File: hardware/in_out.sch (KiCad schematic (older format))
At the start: 33 parts, among them P2 CONN_8, Q4 MMBT2222AT, Q5 MMBT2222AT, Q6 MMBT2222AT, Q7 MMBT2222AT, U6 LTC2635_MSE

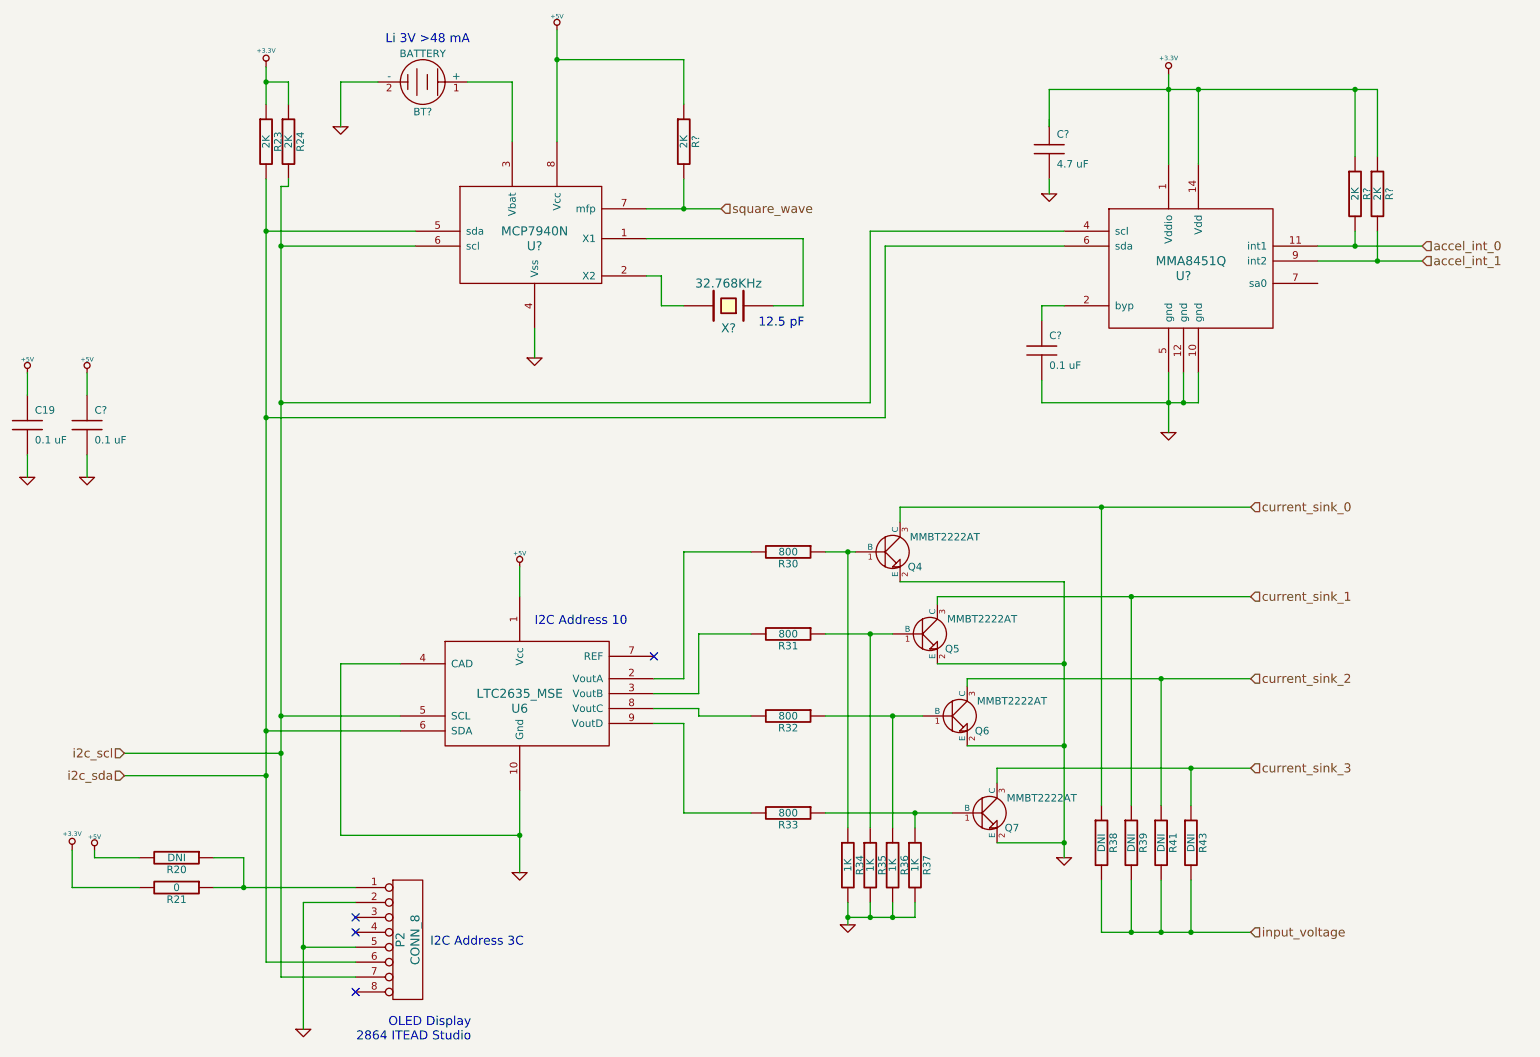
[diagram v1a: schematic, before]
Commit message: fixed some ERCs and simplified reset
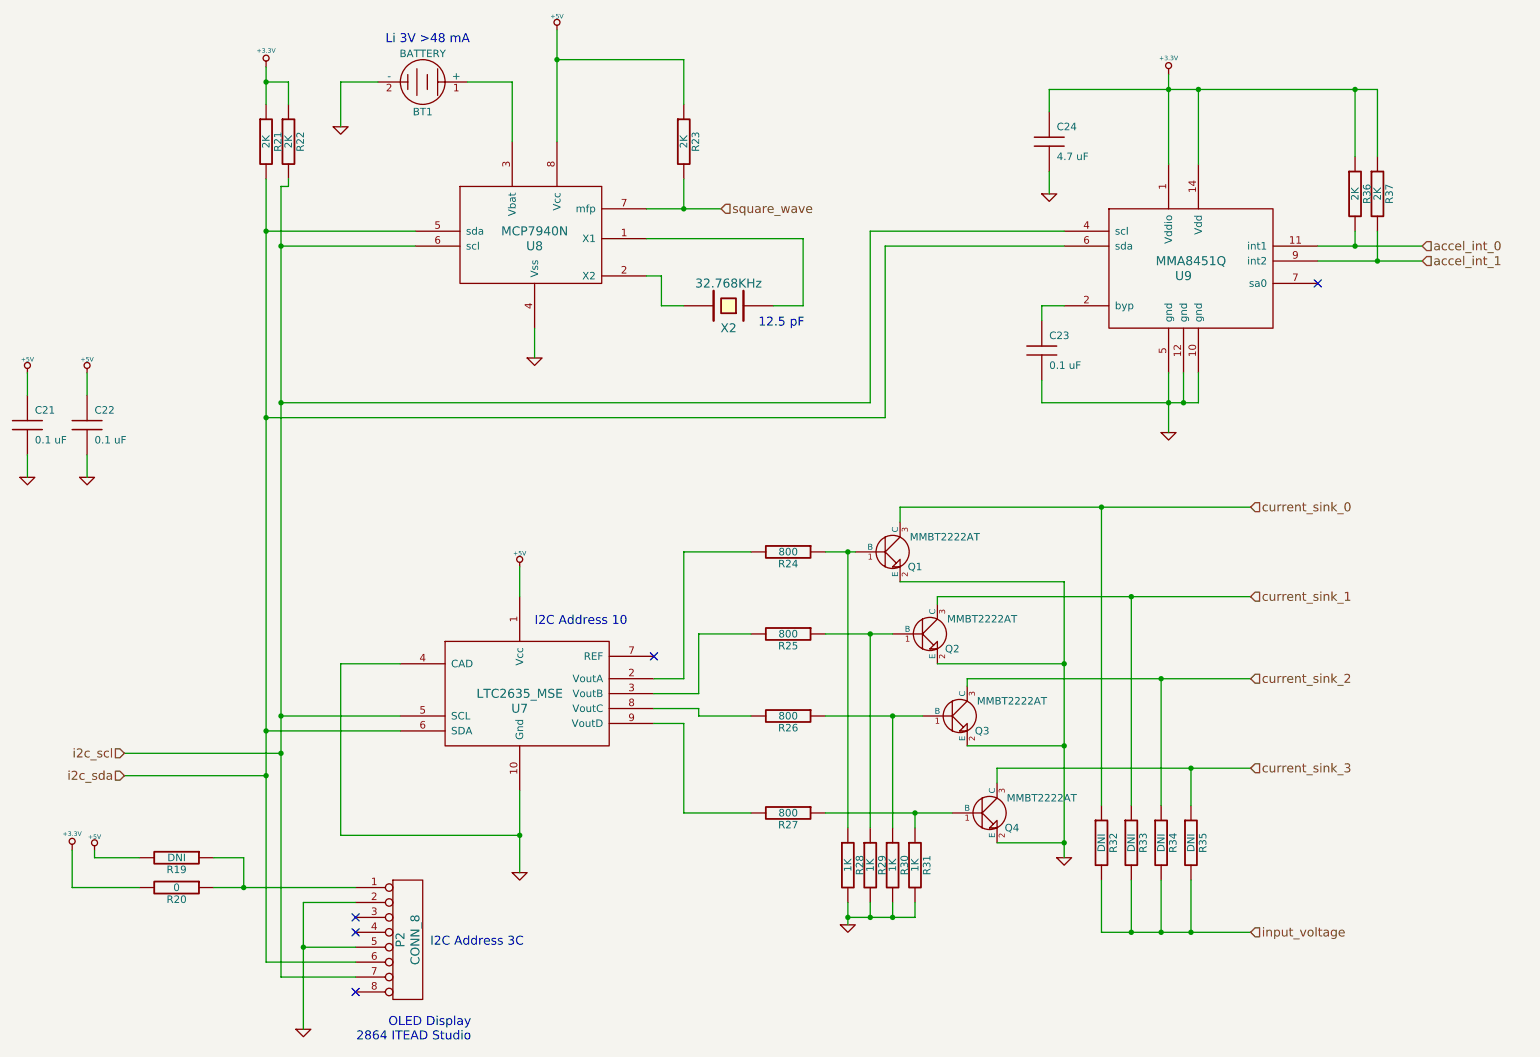
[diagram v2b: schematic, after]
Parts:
- gave numbers to parts that had none: 10
- renumbered C19 to C21, Q4 to Q1, Q5 to Q2, Q6 to Q3, Q7 to Q4, R20 to R19, R21 to R20, R23 to R21, R24 to R22, R30 to R24, R31 to R25, R32 to R26, R33 to R27, R34 to R28, R35 to R29, R36 to R30, R37 to R31, R38 to R32, R39 to R33, R41 to R34, R43 to R35, U6 to U7
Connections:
- net +3.3V: now also C24.1
- no-connect marks 4 -> 5
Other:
- moved on the sheet: C24
